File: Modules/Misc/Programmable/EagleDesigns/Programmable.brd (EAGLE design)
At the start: 100 x 80 mm, 13 parts, among them U2 ATMEGA328P_TQFP

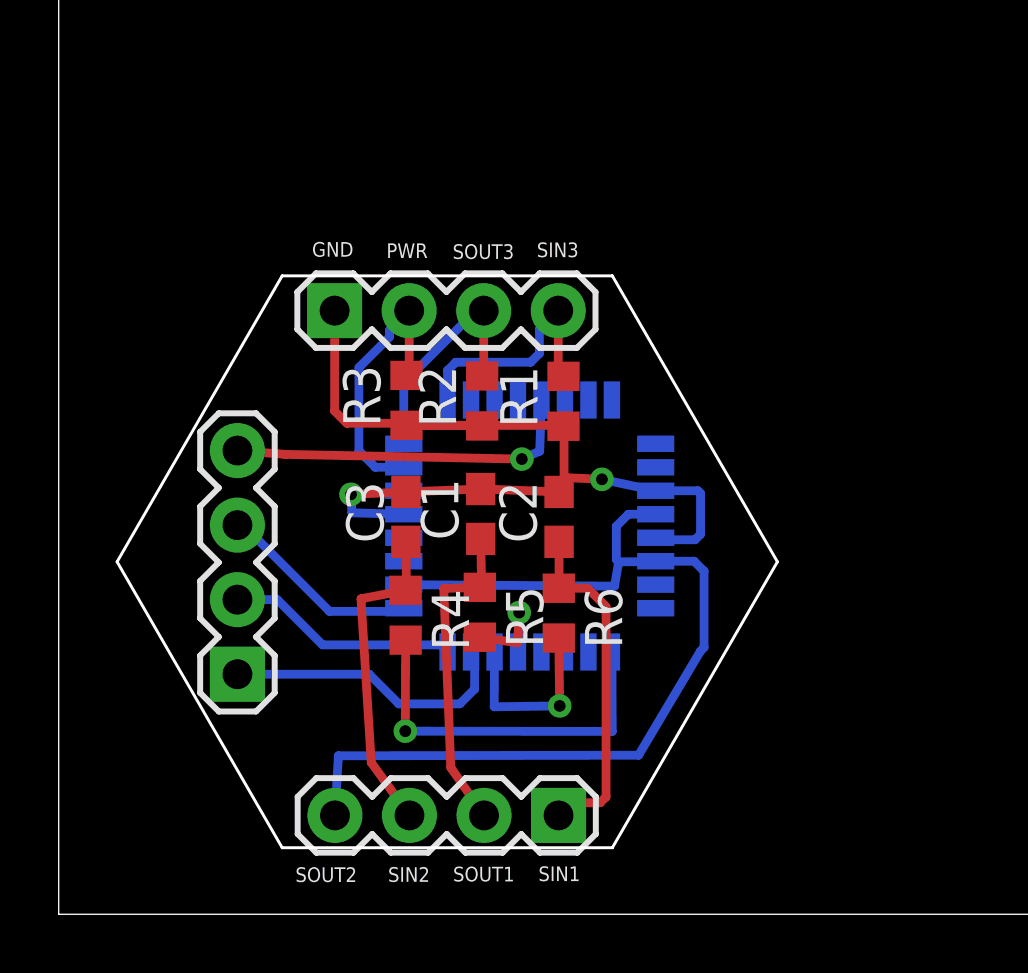
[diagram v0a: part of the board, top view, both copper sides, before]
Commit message: added the programmable module (without OLED display)
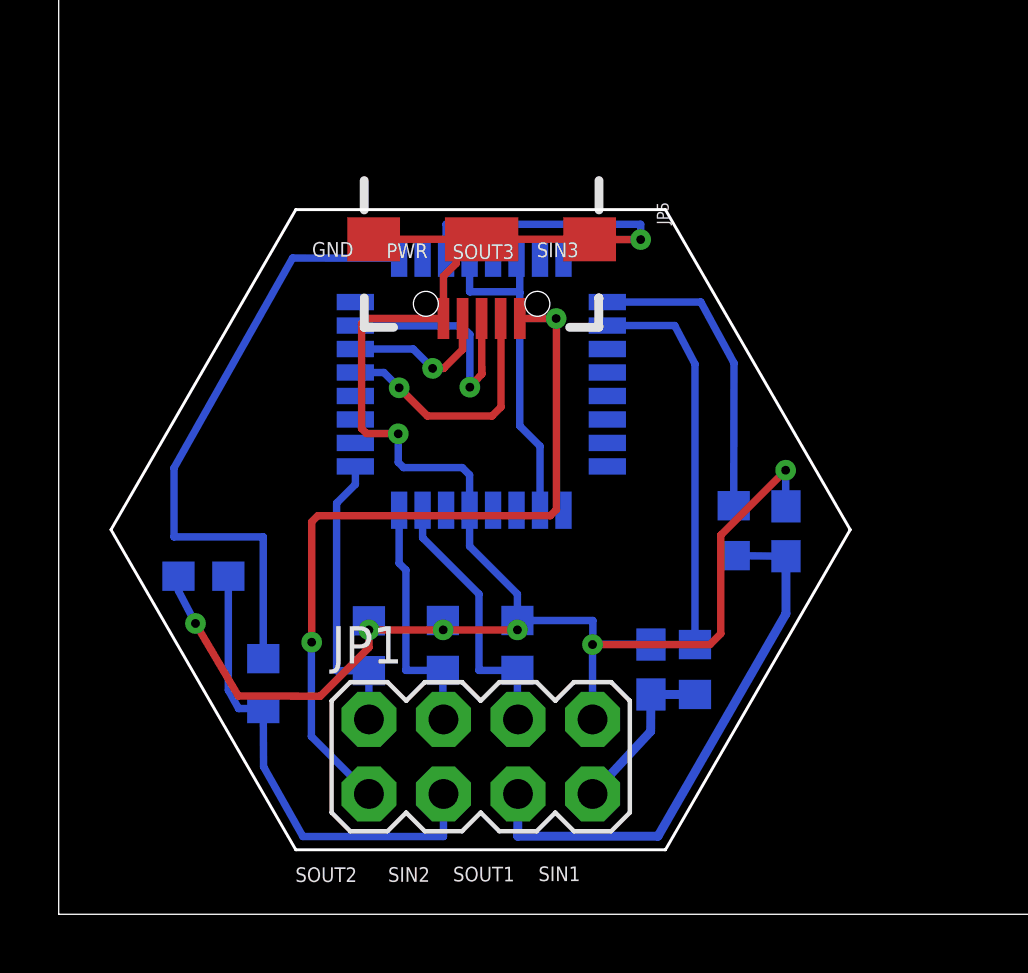
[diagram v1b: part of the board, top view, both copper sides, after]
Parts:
- removed JP2, JP3: (no value), SparkFun-Connectors:1X04
- added JP5: (no value), SparkFun-Connectors:USB-AB-MICRO-SMD_V03
- JP1: device SparkFun-Connectors:1X04 -> SparkFun-Connectors:2X4
- moved R1 10.6 mm to (10.6, 9.15), flipped to the bottom, turned to 270 degrees
- moved C1 10.4 mm to (24.8, 13.1), flipped to the bottom
- moved R3 9.17 mm to (15.6, 9.16), flipped to the bottom, turned to 270 degrees
- moved R5 9.09 mm to (23.0, 13.1), flipped to the bottom, turned to 90 degrees
- moved R2 8.44 mm to (13.1, 9.16), flipped to the bottom, turned to 270 degrees
- moved C3 7.19 mm to (4.93, 11.5), flipped to the bottom, turned to 0 degrees
- moved C2 6.07 mm to (20.2, 8.34), flipped to the bottom
- moved R4 5.38 mm to (6.97, 7.86), flipped to the bottom, turned to 90 degrees
- moved U2 5.10 mm to (14.4, 18.1), turned to 270 degrees
- moved R6 5.02 mm to (21.7, 8.34), flipped to the bottom, turned to 90 degrees
- moved JP1 3.32 mm to (14.4, 5.37), turned to 0 degrees
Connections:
- removed net MISO: JP3.2, U2.16
- removed net MOSI: JP3.1, U2.15
- removed net SCK: JP3.3, U2.17
- new net RX: JP5.ID1, U2.30
- new net TX: JP5.D+1, U2.31
- net GND: now also JP1.8, JP5.GND1, JP5.SHIELD1, JP5.SHIELD2, JP5.SHIELD3; no longer JP2.1
- net OUT1: now also U2.1; no longer U2.9
- net OUT2: now also U2.9; no longer U2.13
- net OUT3: now also U2.10; no longer U2.14
- net RESET: now also JP5.D-1; no longer JP3.4
- net SIN1: now also JP1.6; no longer JP2.2
- net SIN2: now also JP1.4; no longer JP2.3
- net SIN3: now also JP1.2; no longer JP2.4
- net SOUT2: now also JP1.5; no longer JP1.2
- net SOUT3: now also JP1.7; no longer JP1.1
- net VCC: now also JP1.1, JP5.VBUS1; no longer JP1.4
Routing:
- net GND: track 33.9 -> 75.1 mm, vias 2 -> 8
- net MOSI: track 10.0 -> 0.00 mm
- net OUT1: track 12.9 -> 21.4 mm, vias 1 -> 0
- net TX: track 0.00 -> 8.37 mm, vias 0 -> 1
- net MISO: track 7.90 -> 0.00 mm
- net SOUT2: track 11.0 -> 18.7 mm
- net SCK: track 6.93 -> 0.00 mm
- net OUT3: track 6.41 -> 13.3 mm, vias 1 -> 0
- net OUT2: track 3.68 -> 10.4 mm, vias 1 -> 0
- net VCC: track 33.0 -> 39.5 mm, vias 0 -> 2
- net SOUT3: track 11.8 -> 5.67 mm
- net SOUT1: track 11.0 -> 16.4 mm
- net RX: track 0.00 -> 5.25 mm, vias 0 -> 1
- net RESET: track 12.1 -> 8.72 mm
- net SIN3: track 8.41 -> 9.99 mm
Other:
- outline, holes or cut-outs redrawn
